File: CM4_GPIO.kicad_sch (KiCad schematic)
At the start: 8 parts, among them J1601 CM4/5 Module A, J1602 GPIO, SW1601 MSS12C02LS-HB2.0

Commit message: Remove CM4 fan provisions
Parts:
- removed JP1601: Conn_01x03_Male, Connector_PinHeader_2.54mm:PinHeader_1x03_P2.54mm_Vertical_SMD_Pin1Left, symbol Jumper:Jumper_3_Bridged12
- SW2: renamed from SW1601; footprint Hatlabs:SW-SMD_MSS12C02LS-HB2.0-1 -> HL_Button_Switch:SW-SMD_MSS12C02LS-HB2.0-1
- renumbered D1601 to D18, H1601 to H1, J1601 to J10, J1602 to J11, R1601 to R51, R1602 to R52
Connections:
- net GPIO12 is gone; now on net RS485.TXD: J10.31 (GPIO12), J11.32 (Pin_32)
- net GPIO13 is gone; now on net RS485.RXD: J10.28 (GPIO13), J11.33 (Pin_33)
- net RS485.RXD: no longer J10.49 (GPIO18), J11.12 (Pin_12)
- net RS485.TXD: no longer J10.50 (GPIO17), J11.11 (Pin_11)
- new net GPIO17: J10.50 (GPIO17), J11.11 (Pin_11)
- new net GPIO18: J10.49 (GPIO18), J11.12 (Pin_12)
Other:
- note added: "CM5 Module Connector 1/2"
- note removed: "CM4"
- note removed: "CM4/5 Module Connector 1/2"
- note removed: "FAN PWM source selection"

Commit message: Reannotate the board
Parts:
- added BT1: BS-02-A1AJ010, HL_Battery:BatteryHolder-TH_BS-02-A1AJ010, symbol Device:Battery_Cell
- renumbered D18 to D17
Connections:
- net GND: now also BT1.2 (-)
- net VBAT: now also BT1.1 (+)
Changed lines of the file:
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@@
 	(wire
 		(pts
+			(xy 246.38 149.86) (xy 246.38 151.13)
+		)
+		(stroke
+			(width 0)
+			(type solid)
+		)
+	)
+	(wire
+		(pts
 			(xy 255.27 53.34) (xy 257.81 53.34)
 		)
@@
 	(wire
 		(pts
+			(xy 246.38 140.97) (xy 246.38 142.24)
+		)
+		(stroke
+			(width 0)
+			(type default)
+		)
+	)
+	(wire
+		(pts
 			(xy 119.38 71.12) (xy 106.68 71.12)
 		)
@@
 		)
 	)
+	(label "VBAT"
+		(at 246.38 140.97 180)
+		(effects
+			(font
+				(size 1.27 1.27)
+			)
+			(justify right bottom)
+		)
+	)
 	(label "ETH.TD3-"
 		(at 114.3 54.61 0)
@@
 		)
 	)
+	(label "VBAT"
+		(at 54.61 46.99 180)
+		(effects
+			(font
+				(size 1.27 1.27)
+			)
+			(justify right bottom)
+		)
+	)
 	(label "I2C1.SCL"
 		(at 229.87 38.1 0)
@@
 		)
 	)
-	(hierarchical_label "VBAT"
-		(shape input)
-		(at 54.61 46.99 180)
-		(effects
-			(font
-				(size 1.27 1.27)
-			)
-			(justify right)
-		)
-	)
 	(hierarchical_label "CAN{SPI}"
 		(shape bidirectional)
@@
 		(polyline
 			(pts
-				(xy 52.07 82.55) (xy 54.61 82.55) (xy 54.61 140.97) (xy 52.07 140.97)
+				(xy 113.03 143.51) (xy 110.49 143.51) (xy 110.49 68.58) (xy 113.03 68.58)
 			)
 			(stroke
@@
 		(polyline
 			(pts
-				(xy 113.03 143.51) (xy 110.49 143.51) (xy 110.49 68.58) (xy 113.03 68.58)
+				(xy 52.07 82.55) (xy 54.61 82.55) (xy 54.61 140.97) (xy 52.07 140.97)
 			)
 			(stroke
@@
 		(dnp no)
 		(fields_autoplaced yes)
-		(property "Reference" "#PWR094"
+		(property "Reference" "#PWR089"
 			(at 231.14 36.83 0)
 			(effects
@@
 			(project ""
 				(path "/abc482bd-3f17-4d35-80db-1da3dcdb5c27/7c248bd3-8232-4777-a40c-eab53460cf85"
-					(reference "#PWR094")
+					(reference "#PWR089")
 					(unit 1)
 				)
@@
 		(on_board yes)
 		(dnp no)
-		(property "Reference" "#PWR098"
+		(property "Reference" "#PWR094"
 			(at 256.54 88.9 0)
 			(effects
@@
 			(project "HALPI2"
 				(path "/abc482bd-3f17-4d35-80db-1da3dcdb5c27/7c248bd3-8232-4777-a40c-eab53460cf85"
-					(reference "#PWR098")
+					(reference "#PWR094")
 					(unit 1)
 				)
@@
 		(dnp no)
 		(fields_autoplaced yes)
-		(property "Reference" "#PWR093"
+		(property "Reference" "#PWR088"
 			(at 114.3 34.29 0)
 			(effects
@@
 			(project "Yellow"
 				(path "/abc482bd-3f17-4d35-80db-1da3dcdb5c27/7c248bd3-8232-4777-a40c-eab53460cf85"
-					(reference "#PWR093")
+					(reference "#PWR088")
 					(unit 1)
 				)
@@
 		(on_board yes)
 		(dnp no)
-		(property "Reference" "#PWR0100"
+		(property "Reference" "#PWR096"
 			(at 266.7 120.65 0)
 			(effects
@@
 			(project "HALPI2"
 				(path "/abc482bd-3f17-4d35-80db-1da3dcdb5c27/7c248bd3-8232-4777-a40c-eab53460cf85"
-					(reference "#PWR0100")
+					(reference "#PWR096")
 					(unit 1)
 				)
@@
 		(dnp no)
 		(fields_autoplaced yes)
-		(property "Reference" "#PWR099"
+		(property "Reference" "#PWR095"
 			(at 261.62 36.83 0)
 			(effects
@@
 			(project "HALPI2"
 				(path "/abc482bd-3f17-4d35-80db-1da3dcdb5c27/7c248bd3-8232-4777-a40c-eab53460cf85"
-					(reference "#PWR099")
+					(reference "#PWR095")
 					(unit 1)
 				)
@@
 		(dnp no)
 		(fields_autoplaced yes)
-		(property "Reference" "#PWR091"
+		(property "Reference" "#PWR086"
 			(at 83.82 29.21 0)
 			(effects
@@
 			(project "Yellow"
 				(path "/abc482bd-3f17-4d35-80db-1da3dcdb5c27/7c248bd3-8232-4777-a40c-eab53460cf85"
-					(reference "#PWR091")
+					(reference "#PWR086")
 					(unit 1)
 				)
@@
 		(dnp no)
 		(fields_autoplaced yes)
-		(property "Reference" "D18"
+		(property "Reference" "D17"
 			(at 236.22 106.9974 90)
 			(effects
@@
 			(project "HALPI2"
 				(path "/abc482bd-3f17-4d35-80db-1da3dcdb5c27/7c248bd3-8232-4777-a40c-eab53460cf85"
-					(reference "D18")
+					(reference "D17")
 					(unit 1)
 				)
@@
 		(on_board yes)
 		(dnp no)
-		(property "Reference" "#PWR092"
+		(property "Reference" "#PWR087"
 			(at 109.22 34.29 0)
 			(effects
@@
 			(project "Yellow"
 				(path "/abc482bd-3f17-4d35-80db-1da3dcdb5c27/7c248bd3-8232-4777-a40c-eab53460cf85"
-					(reference "#PWR092")
+					(reference "#PWR087")
 					(unit 1)
 				)
@@
 		(on_board yes)
 		(dnp no)
-		(property "Reference" "#PWR090"
+		(property "Reference" "#PWR085"
 			(at 81.28 157.48 0)
 			(effects
@@
 			(project "Yellow"
 				(path "/abc482bd-3f17-4d35-80db-1da3dcdb5c27/7c248bd3-8232-4777-a40c-eab53460cf85"
-					(reference "#PWR090")
+					(reference "#PWR085")
 					(unit 1)
 				)
@@
 		(on_board yes)
 		(dnp no)
-		(property "Reference" "#PWR089"
+		(property "Reference" "#PWR084"
 			(at 78.74 29.21 0)
 			(effects
@@
 			(project "Yellow"
 				(path "/abc482bd-3f17-4d35-80db-1da3dcdb5c27/7c248bd3-8232-4777-a40c-eab53460cf85"
-					(reference "#PWR089")
+					(reference "#PWR084")
+					(unit 1)
+				)
+			)
+		)
+	)
+	(symbol
+		(lib_id "power:GND")
+		(at 246.38 151.13 0)
+		(unit 1)
+		(exclude_from_sim no)
+		(in_bom yes)
+		(on_board yes)
+		(dnp no)
+		(property "Reference" "#PWR092"
+			(at 246.38 157.48 0)
+			(effects
+				(font
+					(size 1.27 1.27)
+				)
+				(hide yes)
+			)
+		)
+		(property "Value" "GND"
+			(at 247.015 155.575 0)
+			(effects
+				(font
+					(size 1.27 1.27)
+				)
+			)
+		)
+		(property "Footprint" ""
+			(at 246.38 151.13 0)
+			(effects
+				(font
+					(size 1.27 1.27)
+				)
+				(hide yes)
+			)
+		)
+		(property "Datasheet" ""
+			(at 246.38 151.13 0)
+			(effects
+				(font
+					(size 1.27 1.27)
+				)
+				(hide yes)
+			)
+		)
+		(property "Description" "Power symbol creates a global label with name \"GND\" , ground"
+			(at 246.38 151.13 0)
+			(effects
+				(font
+					(size 1.27 1.27)
+				)
+				(hide yes)
+			)
+		)
+		(pin "1"
+		)
+		(instances
+			(project "HALPI2"
+				(path "/abc482bd-3f17-4d35-80db-1da3dcdb5c27/7c248bd3-8232-4777-a40c-eab53460cf85"
+					(reference "#PWR092")
 					(unit 1)
 				)
@@
 		(dnp no)
 		(fields_autoplaced yes)
-		(property "Reference" "#PWR095"
+		(property "Reference" "#PWR090"
 			(at 232.41 106.68 0)
 			(effects
@@
 			(project "HALPI2"
 				(path "/abc482bd-3f17-4d35-80db-1da3dcdb5c27/7c248bd3-8232-4777-a40c-eab53460cf85"
-					(reference "#PWR095")
+					(reference "#PWR090")
 					(unit 1)
 				)
@@
 	)
 	(symbol
+		(lib_id "Device:Battery_Cell")
+		(at 246.38 147.32 0)
+		(mirror y)
+		(unit 1)
+		(exclude_from_sim no)
+		(in_bom yes)
+		(on_board yes)
+		(dnp no)
+		(property "Reference" "BT1"
+			(at 243.205 145.415 0)
+			(effects
+				(font
+					(size 1.27 1.27)
+				)
+				(justify left)
+			)
+		)
+		(property "Value" "BS-02-A1AJ010"
+			(at 243.205 147.955 0)
+			(effects
+				(font
+					(size 1.27 1.27)
+				)
+				(justify left)
+			)
+		)
+		(property "Footprint" "HL_Battery:BatteryHolder-TH_BS-02-A1AJ010"
+			(at 246.38 145.796 90)
+			(effects
+				(font
+					(size 1.27 1.27)
+				)
+				(hide yes)
+			)
+		)
+		(property "Datasheet" "~"
+			(at 246.38 145.796 90)
+			(effects
+				(font
+					(size 1.27 1.27)
+				)
+				(hide yes)
+			)
+		)
+		(property "Description" "Single-cell battery"
+			(at 246.38 147.32 0)
+			(effects
+				(font
+					(size 1.27 1.27)
+				)
+				(hide yes)
+			)
+		)
+		(property "LCSC" "C5239862"
+			(at 246.38 147.32 0)
+			(effects
+				(font
+					(size 1.27 1.27)
+				)
+				(hide yes)
+			)
+		)
+		(property "Characteristics" ""
+			(at 246.38 147.32 0)
+			(effects
+				(font
+					(size 1.27 1.27)
+				)
+				(hide yes)
+			)
+		)
+		(property "LCSC Part" ""
+			(at 246.38 147.32 0)
+			(effects
+				(font
+					(size 1.27 1.27)
+				)
+			)
+		)
+		(pin "1"
+		)
+		(pin "2"
+		)
+		(instances
+			(project "HALPI2"
+				(path "/abc482bd-3f17-4d35-80db-1da3dcdb5c27/7c248bd3-8232-4777-a40c-eab53460cf85"
+					(reference "BT1")
+					(unit 1)
+				)
+			)
+		)
+	)
+	(symbol
 		(lib_id "power:GND")
 		(at 241.3 82.55 0)
@@
 		(on_board yes)
 		(dnp no)
-		(property "Reference" "#PWR096"
+		(property "Reference" "#PWR091"
 			(at 241.3 88.9 0)
 			(effects
@@
 			(project "HALPI2"
 				(path "/abc482bd-3f17-4d35-80db-1da3dcdb5c27/7c248bd3-8232-4777-a40c-eab53460cf85"
-					(reference "#PWR096")
+					(reference "#PWR091")
 					(unit 1)
 				)
@@
 		(on_board yes)
 		(dnp no)
-		(property "Reference" "#PWR097"
+		(property "Reference" "#PWR093"
 			(at 250.19 125.73 0)
 			(effects
@@
 			(project "HALPI2"
 				(path "/abc482bd-3f17-4d35-80db-1da3dcdb5c27/7c248bd3-8232-4777-a40c-eab53460cf85"
-					(reference "#PWR097")
+					(reference "#PWR093")
 					(unit 1)
 				)

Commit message: Fix DRC issues
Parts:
- added D43: 1N4148WT, Diode_SMD:D_SOD-523, symbol Device:D_Small
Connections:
- net nRPIBOOT: now also D43.2 (A); no longer R52.1, SW2.2
- new net: D43.1 (K), R52.1, SW2.2

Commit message: Add GND/3.3V/5V headers, add missing JLC part numbers
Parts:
- added TP64: TestPoint, TestPoint:TestPoint_Pad_D1.0mm, symbol Connector:TestPoint
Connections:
- net at SW2.1: now also TP64.1
- no-connect marks 13 -> 12
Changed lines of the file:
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@@
 	)
 	(no_connect
-		(at 250.19 107.95)
-	)
-	(no_connect
 		(at 55.88 72.39)
 	)
@@
 	(wire
 		(pts
+			(xy 250.19 107.95) (xy 247.65 107.95)
+		)
+		(stroke
+			(width 0)
+			(type default)
+		)
+	)
+	(wire
+		(pts
 			(xy 255.27 73.66) (xy 256.54 73.66)
 		)
@@
 	(wire
 		(pts
+			(xy 247.65 107.95) (xy 247.65 104.14)
+		)
+		(stroke
+			(width 0)
+			(type default)
+		)
+	)
+	(wire
+		(pts
 			(xy 256.54 55.88) (xy 255.27 55.88)
 		)
@@
 					(unit 1)
 				)
+			)
+		)
+	)
+	(symbol
+		(lib_id "Connector:TestPoint")
+		(at 247.65 104.14 0)
+		(unit 1)
+		(exclude_from_sim no)
+		(in_bom yes)
+		(on_board yes)
+		(dnp no)
+		(property "Reference" "TP64"
+			(at 245.11 99.5679 0)
+			(effects
+				(font
+					(size 1.27 1.27)
+				)
+				(justify right)
+			)
+		)
+		(property "Value" "TestPoint"
+			(at 245.11 102.1079 0)
+			(effects
+				(font
+					(size 1.27 1.27)
+				)
+				(justify right)
+			)
+		)
+		(property "Footprint" "TestPoint:TestPoint_Pad_D1.0mm"
+			(at 252.73 104.14 0)
+			(effects
+				(font
+					(size 1.27 1.27)
+				)
+				(hide yes)
+			)
+		)
+		(property "Datasheet" "~"
+			(at 252.73 104.14 0)
+			(effects
+				(font
+					(size 1.27 1.27)
+				)
+				(hide yes)
+			)
+		)
+		(property "Description" "test point"
+			(at 247.65 104.14 0)
+			(effects
+				(font
+					(size 1.27 1.27)
+				)
+				(hide yes)
+			)
+		)
+		(property "Characteristics" ""
+			(at 247.65 104.14 0)
+			(effects
+				(font
+					(size 1.27 1.27)
+				)
+				(hide yes)
+			)
+		)
+		(property "LCSC Part" ""
+			(at 247.65 104.14 0)
+			(effects
+				(font
+					(size 1.27 1.27)
+				)
+			)
+		)
+		(property "Field8" ""
+			(at 247.65 104.14 0)
+			(effects
+				(font
+					(size 1.27 1.27)
+				)
+			)
+		)
+		(property "PartNumber" ""
+			(at 247.65 104.14 0)
+			(effects
+				(font
+					(size 1.27 1.27)
+				)
+			)
+		)
+		(pin "1"
+		)
+		(instances
+			(project "HALPI2"
+				(path "/abc482bd-3f17-4d35-80db-1da3dcdb5c27/7c248bd3-8232-4777-a40c-eab53460cf85"
+					(reference "TP64")
+					(unit 1)
+				)

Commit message: FInal v0.2.0 proto changes
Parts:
- D16: renamed from D43; JLCPCB_CORRECTION (none) -> 0;0;180
- renumbered TP64 to TP34
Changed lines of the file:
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@@
 	)
 	(junction
+		(at 246.38 142.24)
+		(diameter 0)
+		(color 0 0 0 0)
+	)
+	(junction
 		(at 256.54 68.58)
 		(diameter 1.016)
@@
 		(polyline
 			(pts
-				(xy 113.03 143.51) (xy 110.49 143.51) (xy 110.49 68.58) (xy 113.03 68.58)
+				(xy 44.45 39.37) (xy 46.99 39.37) (xy 46.99 64.77) (xy 44.45 64.77)
 			)
 			(stroke
@@
 		(polyline
 			(pts
-				(xy 52.07 82.55) (xy 54.61 82.55) (xy 54.61 140.97) (xy 52.07 140.97)
+				(xy 124.46 36.83) (xy 127 36.83) (xy 127 60.96) (xy 124.46 60.96)
 			)
 			(stroke
@@
 		(polyline
 			(pts
-				(xy 44.45 39.37) (xy 46.99 39.37) (xy 46.99 64.77) (xy 44.45 64.77)
+				(xy 52.07 82.55) (xy 54.61 82.55) (xy 54.61 140.97) (xy 52.07 140.97)
 			)
 			(stroke
@@
 		(polyline
 			(pts
-				(xy 124.46 36.83) (xy 127 36.83) (xy 127 60.96) (xy 124.46 60.96)
+				(xy 113.03 143.51) (xy 110.49 143.51) (xy 110.49 68.58) (xy 113.03 68.58)
 			)
 			(stroke
@@
 	)
 	(symbol
+		(lib_id "power:PWR_FLAG")
+		(at 246.38 142.24 270)
+		(unit 1)
+		(exclude_from_sim no)
+		(in_bom yes)
+		(on_board yes)
+		(dnp no)
+		(fields_autoplaced yes)
+		(property "Reference" "#FLG025"
+			(at 248.285 142.24 0)
+			(effects
+				(font
+					(size 1.27 1.27)
+				)
+				(hide yes)
+			)
+		)
+		(property "Value" "PWR_FLAG"
+			(at 250.19 142.2399 90)
+			(effects
+				(font
+					(size 1.27 1.27)
+				)
+				(justify left)
+			)
+		)
+		(property "Footprint" ""
+			(at 246.38 142.24 0)
+			(effects
+				(font
+					(size 1.27 1.27)
+				)
+				(hide yes)
+			)
+		)
+		(property "Datasheet" "~"
+			(at 246.38 142.24 0)
+			(effects
+				(font
+					(size 1.27 1.27)
+				)
+				(hide yes)
+			)
+		)
+		(property "Description" "Special symbol for telling ERC where power comes from"
+			(at 246.38 142.24 0)
+			(effects
+				(font
+					(size 1.27 1.27)
+				)
+				(hide yes)
+			)
+		)
+		(pin "1"
+		)
+		(instances
+			(project ""
+				(path "/abc482bd-3f17-4d35-80db-1da3dcdb5c27/7c248bd3-8232-4777-a40c-eab53460cf85"
+					(reference "#FLG025")
+					(unit 1)
+				)
+			)
+		)
+	)
+	(symbol
 		(lib_id "Hatlabs:+3.3VCMx")
 		(at 231.14 33.02 0)
@@
 		(dnp no)
 		(fields_autoplaced yes)
-		(property "Reference" "#PWR089"
+		(property "Reference" "#PWR090"
 			(at 231.14 36.83 0)
 			(effects
@@
 			(project ""
 				(path "/abc482bd-3f17-4d35-80db-1da3dcdb5c27/7c248bd3-8232-4777-a40c-eab53460cf85"
-					(reference "#PWR089")
+					(reference "#PWR090")
 					(unit 1)
 				)
@@
 		(on_board yes)
 		(dnp no)
-		(property "Reference" "#PWR094"
+		(property "Reference" "#PWR095"
 			(at 256.54 88.9 0)
 			(effects
@@
 			(project "HALPI2"
 				(path "/abc482bd-3f17-4d35-80db-1da3dcdb5c27/7c248bd3-8232-4777-a40c-eab53460cf85"
-					(reference "#PWR094")
+					(reference "#PWR095")
 					(unit 1)
 				)
@@
 		(dnp no)
 		(fields_autoplaced yes)
-		(property "Reference" "#PWR088"
+		(property "Reference" "#PWR089"
 			(at 114.3 34.29 0)
 			(effects
@@
 			(project "Yellow"
 				(path "/abc482bd-3f17-4d35-80db-1da3dcdb5c27/7c248bd3-8232-4777-a40c-eab53460cf85"
-					(reference "#PWR088")
+					(reference "#PWR089")
 					(unit 1)
 				)
@@
 		(on_board yes)
 		(dnp no)
-		(property "Reference" "#PWR096"
+		(property "Reference" "#PWR097"
 			(at 266.7 120.65 0)
 			(effects
@@
 			(project "HALPI2"
 				(path "/abc482bd-3f17-4d35-80db-1da3dcdb5c27/7c248bd3-8232-4777-a40c-eab53460cf85"
-					(reference "#PWR096")
+					(reference "#PWR097")
 					(unit 1)
 				)
@@
 		(dnp no)
 		(fields_autoplaced yes)
-		(property "Reference" "#PWR095"
+		(property "Reference" "#PWR096"
 			(at 261.62 36.83 0)
 			(effects
@@
 			(project "HALPI2"
 				(path "/abc482bd-3f17-4d35-80db-1da3dcdb5c27/7c248bd3-8232-4777-a40c-eab53460cf85"
-					(reference "#PWR095")
+					(reference "#PWR096")
 					(unit 1)
 				)
@@
 		(dnp no)
 		(fields_autoplaced yes)
-		(property "Reference" "#PWR086"
+		(property "Reference" "#PWR087"
 			(at 83.82 29.21 0)
 			(effects
@@
 			(project "Yellow"
 				(path "/abc482bd-3f17-4d35-80db-1da3dcdb5c27/7c248bd3-8232-4777-a40c-eab53460cf85"
-					(reference "#PWR086")
+					(reference "#PWR087")
 					(unit 1)
 				)
@@
 		(on_board yes)
 		(dnp no)
-		(property "Reference" "TP64"
+		(property "Reference" "TP34"
 			(at 245.11 99.5679 0)
 			(effects
@@
 			)
 		)
+		(property "Sim.Enable" ""
+			(at 247.65 104.14 0)
+			(effects
+				(font
+					(size 1.27 1.27)
+				)
+			)
+		)
 		(pin "1"
 		)
@@
 			(project "HALPI2"
 				(path "/abc482bd-3f17-4d35-80db-1da3dcdb5c27/7c248bd3-8232-4777-a40c-eab53460cf85"
-					(reference "TP64")
+					(reference "TP34")
 					(unit 1)
 				)
@@
 		(on_board yes)
 		(dnp no)
-		(property "Reference" "#PWR087"
+		(property "Reference" "#PWR088"
 			(at 109.22 34.29 0)
 			(effects
@@
 			(project "Yellow"
 				(path "/abc482bd-3f17-4d35-80db-1da3dcdb5c27/7c248bd3-8232-4777-a40c-eab53460cf85"
-					(reference "#PWR087")
+					(reference "#PWR088")
 					(unit 1)
 				)
@@
 		(on_board yes)
 		(dnp no)
-		(property "Reference" "#PWR085"
+		(property "Reference" "#PWR086"
 			(at 81.28 157.48 0)
 			(effects
@@
 			(project "Yellow"
 				(path "/abc482bd-3f17-4d35-80db-1da3dcdb5c27/7c248bd3-8232-4777-a40c-eab53460cf85"
-					(reference "#PWR085")
+					(reference "#PWR086")
 					(unit 1)
 				)
@@
 		(on_board yes)
 		(dnp no)
-		(property "Reference" "#PWR084"
+		(property "Reference" "#PWR085"
 			(at 78.74 29.21 0)
 			(effects
@@
 			(project "Yellow"
 				(path "/abc482bd-3f17-4d35-80db-1da3dcdb5c27/7c248bd3-8232-4777-a40c-eab53460cf85"
-					(reference "#PWR084")
+					(reference "#PWR085")
 					(unit 1)
 				)
@@
 		(on_board yes)
 		(dnp no)
-		(property "Reference" "#PWR092"
+		(property "Reference" "#PWR093"
 			(at 246.38 157.48 0)
 			(effects
@@
 			(project "HALPI2"
 				(path "/abc482bd-3f17-4d35-80db-1da3dcdb5c27/7c248bd3-8232-4777-a40c-eab53460cf85"
-					(reference "#PWR092")
+					(reference "#PWR093")
 					(unit 1)
 				)
@@
 		(dnp no)
 		(fields_autoplaced yes)
-		(property "Reference" "D43"
+		(property "Reference" "D16"
 			(at 227.33 115.57 0)
 			(effects
@@
 			)
 		)
+		(property "JLCPCB_CORRECTION" "0;0;180"
+			(at 227.33 121.92 0)
+			(effects
+				(font
+					(size 1.27 1.27)
+				)
+			)
+		)
 		(pin "2"
 		)
@@
 			(project "HALPI2"
 				(path "/abc482bd-3f17-4d35-80db-1da3dcdb5c27/7c248bd3-8232-4777-a40c-eab53460cf85"
-					(reference "D43")
+					(reference "D16")
 					(unit 1)
 				)
@@
 		(dnp no)
 		(fields_autoplaced yes)
-		(property "Reference" "#PWR090"
+		(property "Reference" "#PWR091"
 			(at 232.41 106.68 0)
 			(effects
@@
 			(project "HALPI2"
 				(path "/abc482bd-3f17-4d35-80db-1da3dcdb5c27/7c248bd3-8232-4777-a40c-eab53460cf85"
-					(reference "#PWR090")
+					(reference "#PWR091")
 					(unit 1)
 				)
@@
 		(on_board yes)
 		(dnp no)
-		(property "Reference" "#PWR091"
+		(property "Reference" "#PWR092"
 			(at 241.3 88.9 0)
 			(effects
@@
 			(project "HALPI2"
 				(path "/abc482bd-3f17-4d35-80db-1da3dcdb5c27/7c248bd3-8232-4777-a40c-eab53460cf85"
-					(reference "#PWR091")
+					(reference "#PWR092")
 					(unit 1)
 				)
@@
 		(on_board yes)
 		(dnp no)
-		(property "Reference" "#PWR093"
+		(property "Reference" "#PWR094"
 			(at 250.19 125.73 0)
 			(effects
@@
 			(project "HALPI2"
 				(path "/abc482bd-3f17-4d35-80db-1da3dcdb5c27/7c248bd3-8232-4777-a40c-eab53460cf85"
-					(reference "#PWR093")
+					(reference "#PWR094")
 					(unit 1)
 				)

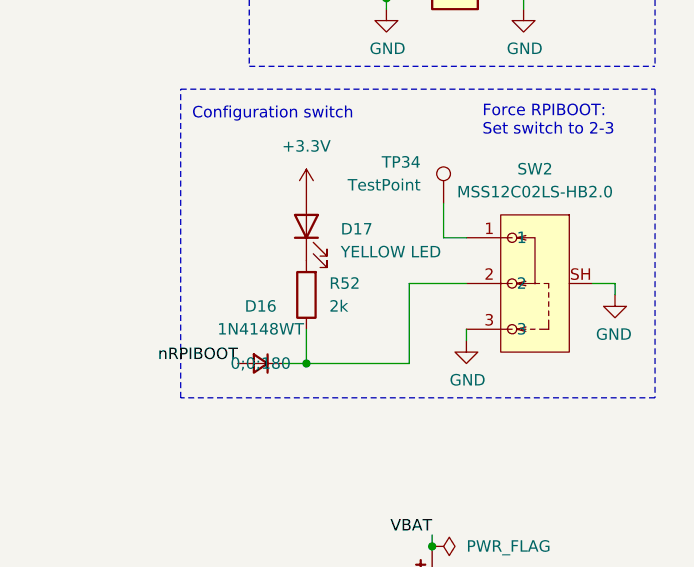
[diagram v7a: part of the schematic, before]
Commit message: Nailed the current limiter design
Also added more GND test pads
Also fixed the MCU I2C pinout
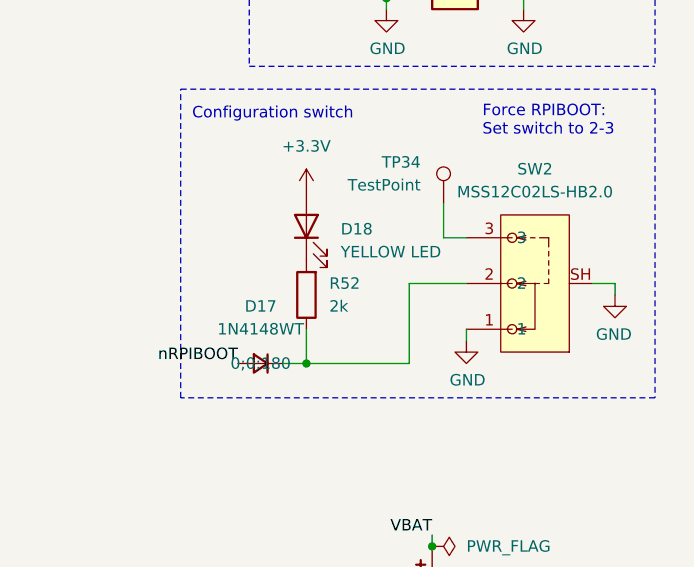
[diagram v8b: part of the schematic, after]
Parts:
- renumbered D16 to D17, D17 to D18
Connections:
- net GND: now also SW2.1; no longer SW2.3
- net at TP34.1: now also SW2.3; no longer SW2.1
